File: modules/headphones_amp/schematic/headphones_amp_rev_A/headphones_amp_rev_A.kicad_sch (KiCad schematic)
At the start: 113 parts, among them J1 AudioJack3_SwitchTR, J2 AudioJack3_SwitchTR, J3 Conn_01x02, J4 Conn_01x02, J5 Conn_01x02, J6 Conn_01x02, J7 Conn_01x02, Q1 BC140, Q10 BC548, Q11 BC548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

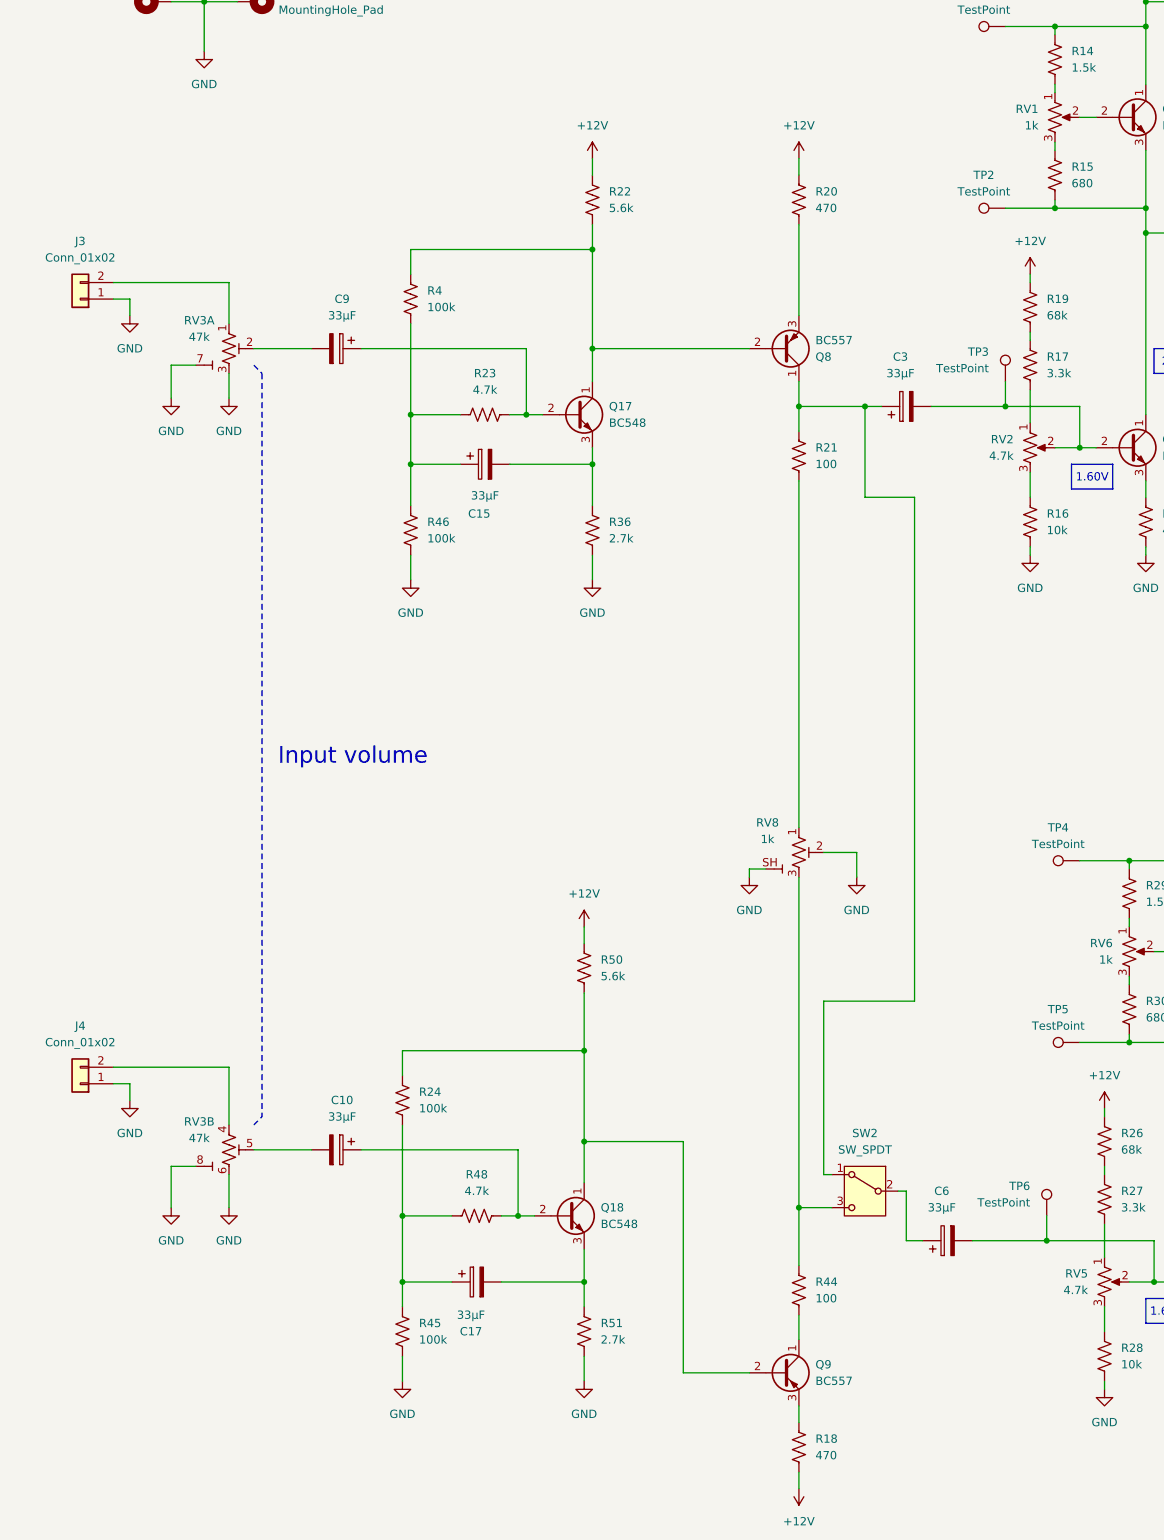
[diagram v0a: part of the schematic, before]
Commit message: added a PDF export of the schematic
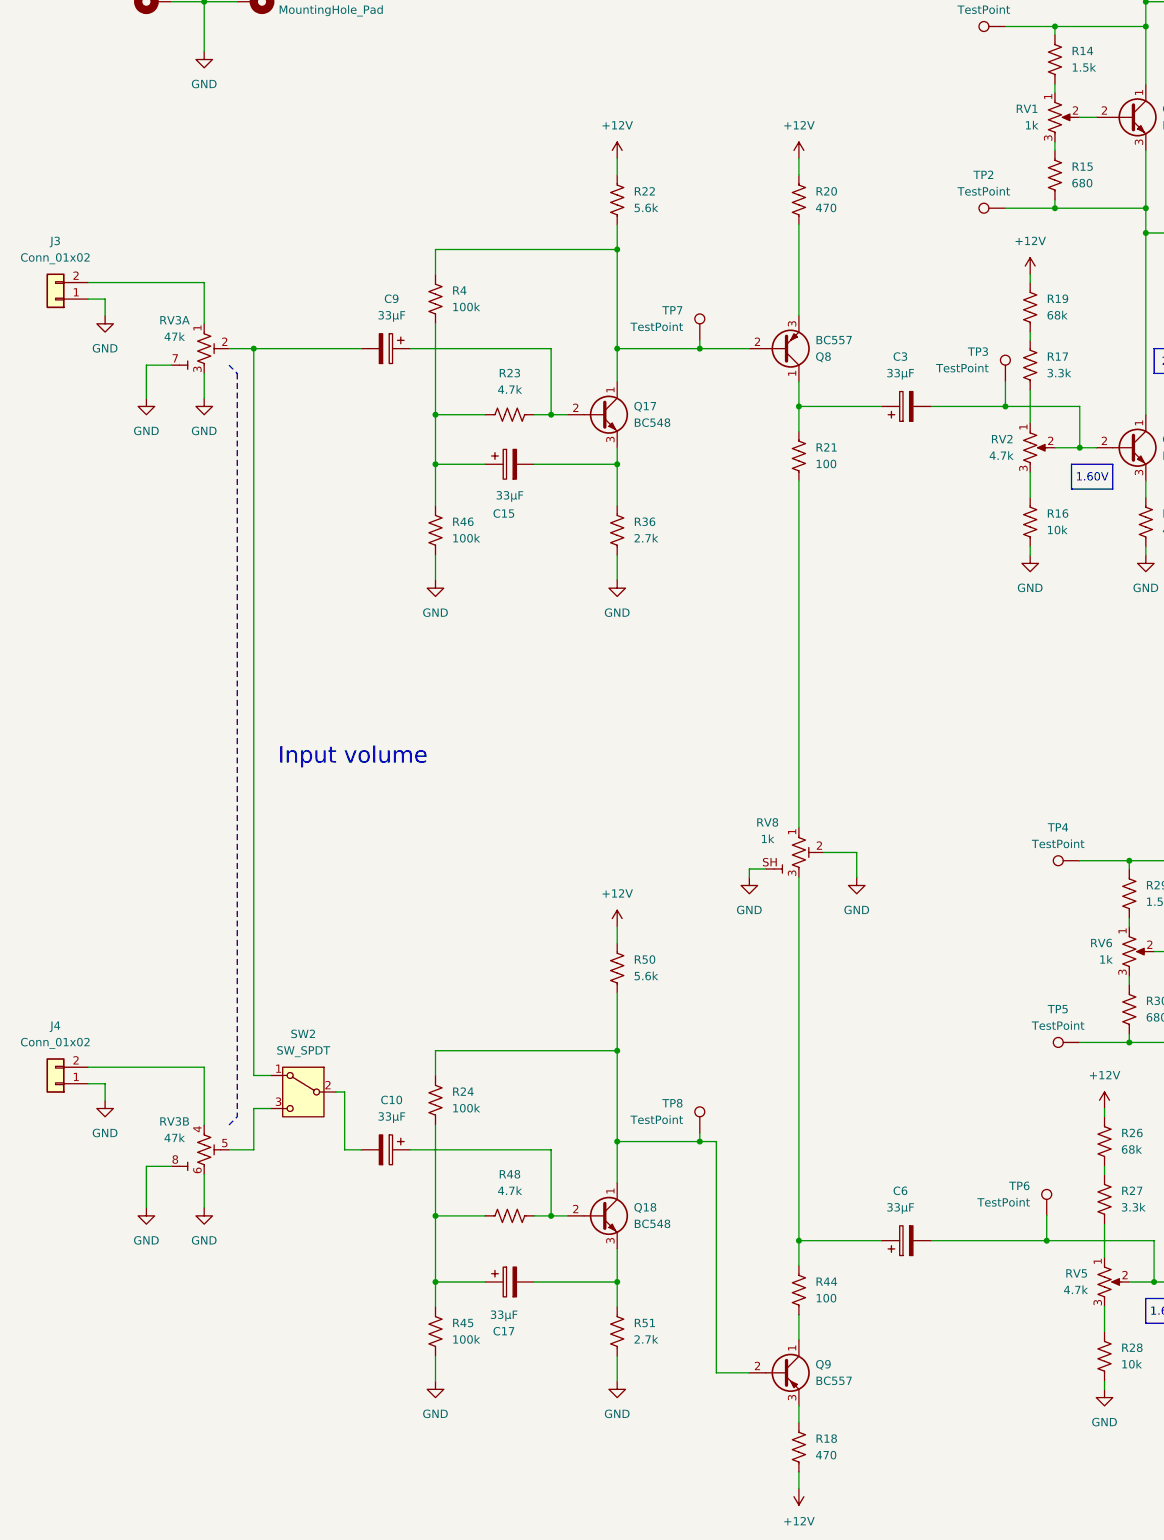
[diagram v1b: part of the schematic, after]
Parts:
- added TP7, TP8: TestPoint, TestPoint:TestPoint_Pad_D2.0mm, symbol Connector:TestPoint
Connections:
- net at Q17.1 (C), Q8.2 (B), R22.2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: now also TP7.1
- net at R44.1, RV8.3 (B): now also C6.1; no longer SW2.3
- net at SW2.2: now also C10.2; no longer C6.1
- net at C3.1, Q8.1 (C), R21.1: no longer SW2.1
- net at Q18.1 (C), Q9.2 (B), R24.1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: now also TP8.1
- net at C9.2, RV3.2 (W): now also SW2.1
- net at RV3.5 (W): now also SW2.3; no longer C10.2
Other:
- moved on the sheet: C10, C15, C17, C6, C9, J3, J4, Q17, Q18, R22, R23, R24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
